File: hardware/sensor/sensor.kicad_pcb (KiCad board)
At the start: 2 copper layers, 32 parts, among them IC1 ATTINY202-SSN, IC2 Si4012-C1001GTR, IC3 TPS3839L30DBZR, J1 M20-9770342

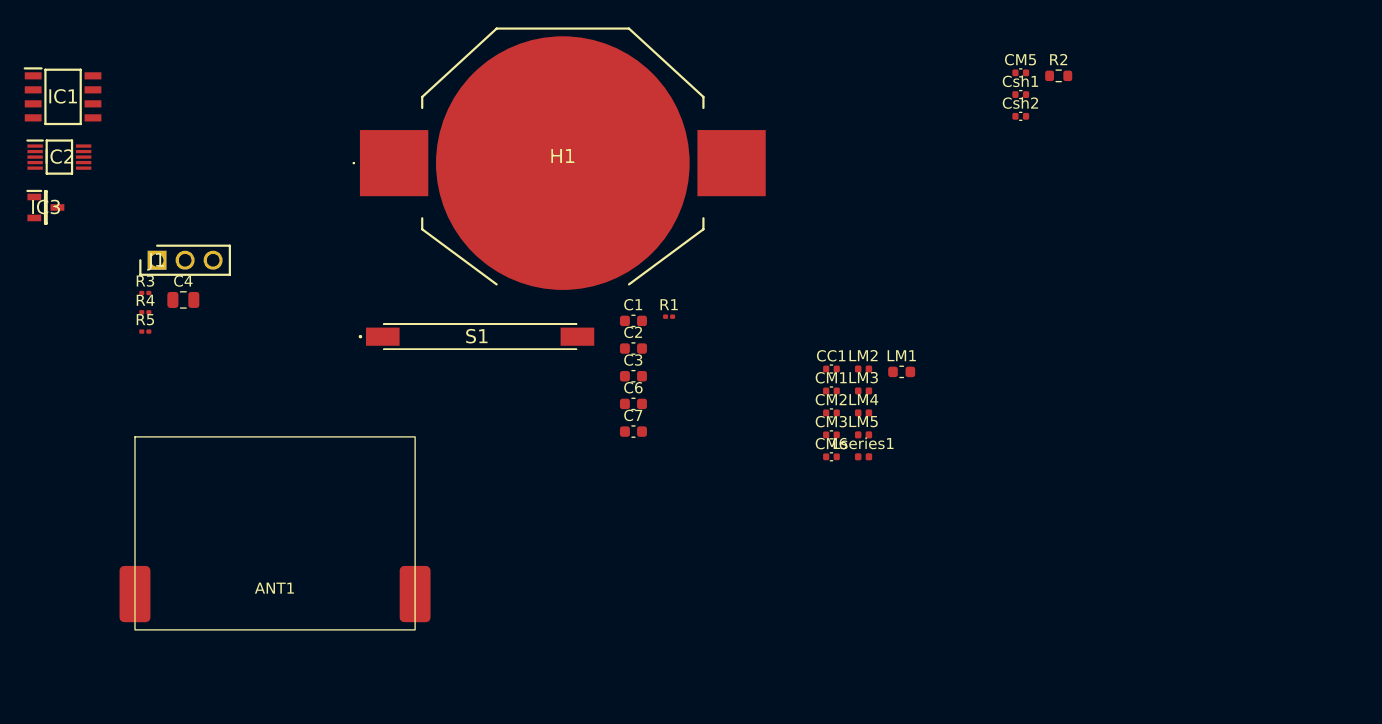
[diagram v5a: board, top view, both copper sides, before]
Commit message: EG-22 Components added to the PCB, no connections, not final position.
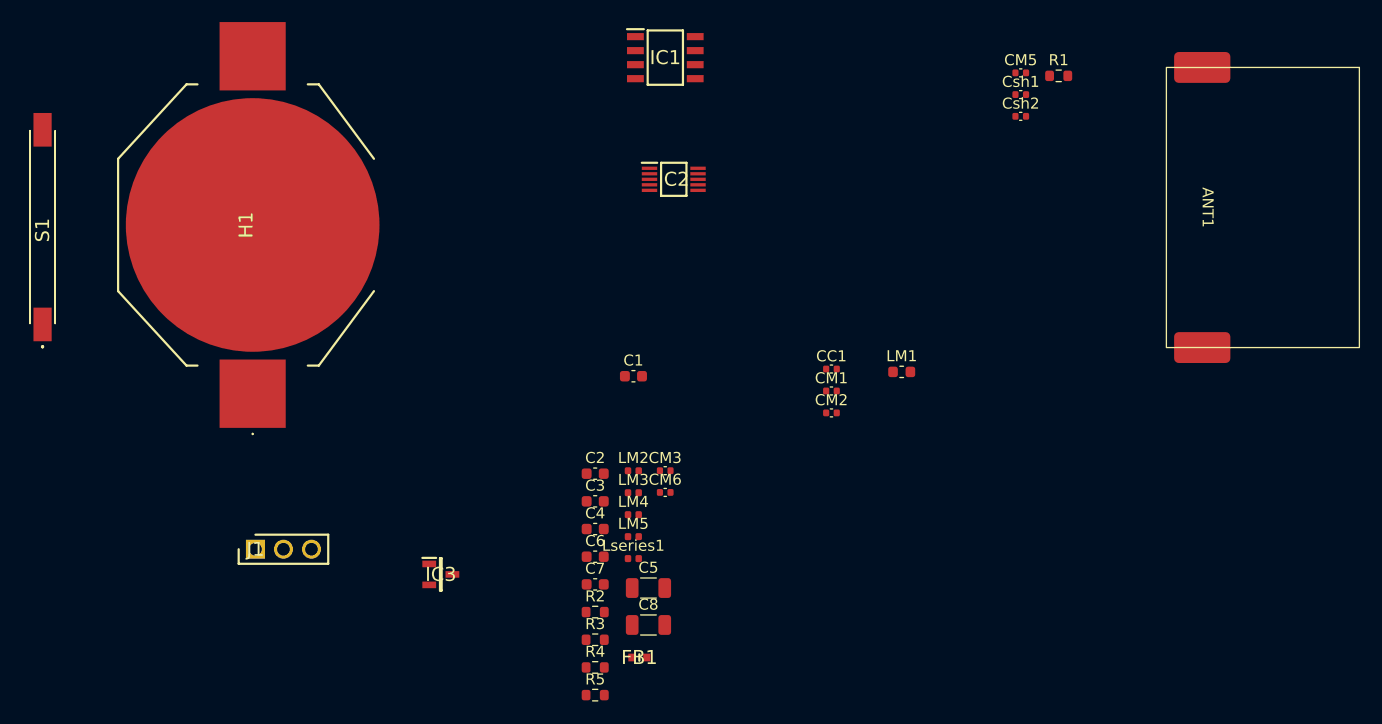
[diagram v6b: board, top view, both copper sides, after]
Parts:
- removed the C1 at (85.8, 46.1)
- removed the R1 at (89.1, 45.7)
- added C3: 1uF, Capacitor_SMD:C_0603_1608Metric, F.Cu at (82.4, 62.5)
- added C5: 47uF, 6.3V, Capacitor_SMD:C_1206_3216Metric, F.Cu at (87.2, 70.3)
- added C8: 47uF, 6.3V, Capacitor_SMD:C_1206_3216Metric, F.Cu at (87.2, 73.7)
- added FB1: BLM18KG601SN1D, MyParts:BLM18SP221SN1B, F.Cu at (86.4, 76.6)
- added R2: 100K, Resistor_SMD:R_0603_1608Metric, F.Cu at (82.4, 72.5)
- C4: value 47uF, 6.3V -> 100nF; footprint Capacitor_SMD:C_0805_2012Metric -> Capacitor_SMD:C_0603_1608Metric
- C7: value 100nF -> 100pF
- R3: value 100K -> 10K; footprint Resistor_SMD:R_0201_0603Metric -> Resistor_SMD:R_0603_1608Metric
- R4: footprint Resistor_SMD:R_0201_0603Metric -> Resistor_SMD:R_0603_1608Metric
- R5: value 10K -> 100K; footprint Resistor_SMD:R_0201_0603Metric -> Resistor_SMD:R_0603_1608Metric
- moved ANT1 91.1 mm to (137.4, 35.8), turned to -90 degrees
- moved IC2 55.7 mm to (89.5, 33.3)
- moved IC1 54.7 mm to (88.7, 22.2)
- moved R5 52.4 mm to (82.4, 80.0)
- moved R4 52.0 mm to (82.4, 77.5)
- moved R3 51.5 mm to (82.4, 75.0)
- moved IC3 48.9 mm to (68.4, 69.1)
- moved C4 42.7 mm to (82.4, 65.0)
- moved S1 40.9 mm to (32.3, 37.6), turned to 90 degrees
- moved H1 28.7 mm to (51.3, 37.4), turned to 90 degrees
- moved J1 27.7 mm to (51.6, 66.8)
- moved LM2 22.8 mm to (85.8, 59.7)
- moved LM3 22.8 mm to (85.8, 61.7)
- moved LM4 22.8 mm to (85.8, 63.7)
- moved LM5 22.8 mm to (85.8, 65.7)
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- renumbered C3 to C1, R2 to R1
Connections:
- C2 pad 1: 3.0V -> WND
- C6 pad 1: 3.0V -> RF_VDD
- C7 pad 1: WND -> RF_VDD
- IC2 pad 5: 3.0V -> RF_VDD
- LM1 pad 1: 3.0V -> RF_VDD
- R3 pad 1: SDN -> 3.0V
- R3 pad 2: 3.0V -> SCL
- R4 pad 1: SCL -> 3.0V
- R4 pad 2: 3.0V -> SDA
- R5 pad 1: SDA -> 3.0V
- R5 pad 2: 3.0V -> SDN
